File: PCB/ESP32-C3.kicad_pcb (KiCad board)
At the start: 2 copper layers, 28.4 x 27.8 mm, 45 parts, among them J1 HCZZ0039-3, J2 DPS_PPS_Right_Angle, SW2 TS4535TP 250gf 009, U1 USB-C-16P-SMD, U2 BQ24072RGT, U3 ESP32-C3, Y1 40MHz_S3240000151040

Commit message: Neuste Version
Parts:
- added D1: XL-1615RGBC-RF, LEDSMD:LED_0606_1432, F.Cu at (145.6, 80.9)
- added R14: 100_0402, Resistor_SMD:R_0402_1005Metric, F.Cu at (145.5, 79.2)
- added R19: 100_0402, Resistor_SMD:R_0402_1005Metric, F.Cu at (147.5, 80.8)
- added R21: 100_0402, Resistor_SMD:R_0402_1005Metric, F.Cu at (145.8, 82.6)
- moved SW2 1.49 mm to (152.5, 72.4), turned to 0 degrees
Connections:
- U3 pad 18: unconnected-(U3-VDD_SPI-Pad18) -> Rot
- U3 pad 23: unconnected-(U3-SPID-Pad23) -> Blau
- U3 pad 24: unconnected-(U3-SPIQ-Pad24) -> Grün
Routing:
- net Grün: track 0.00 -> 23.2 mm, vias 0 -> 2
- net Blau: track 0.00 -> 17.4 mm, vias 0 -> 2
- net Rot: track 0.00 -> 11.2 mm, vias 0 -> 2
- net EXTI: track 28.6 -> 23.7 mm
- net NCHG: track 37.9 -> 41.3 mm
- net Net-(D1-BK): track 0.00 -> 1.25 mm
- net Net-(D1-GK): track 0.00 -> 1.24 mm
- net Net-(D1-RK): track 0.00 -> 1.20 mm
- net MCU_SCL: track 31.2 -> 31.8 mm
- net NPGOOD: track 29.6 -> 30.1 mm
- net GND: track 41.9 -> 41.8 mm, vias 31 -> 28
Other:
- board text added: "+"
- board text added: "-"
- board text added: "A.S. W-Charger 05.2024"
- board text added: "Button"
- board text added: "Cha."
- board text added: "Charging"
- board text added: "GND SCL SDA"
- board text added: "In."
- board text added: "Input"
- board text added: "TEMP"
- board text added: "|"

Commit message: Update
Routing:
- net GND: vias 28 -> 41

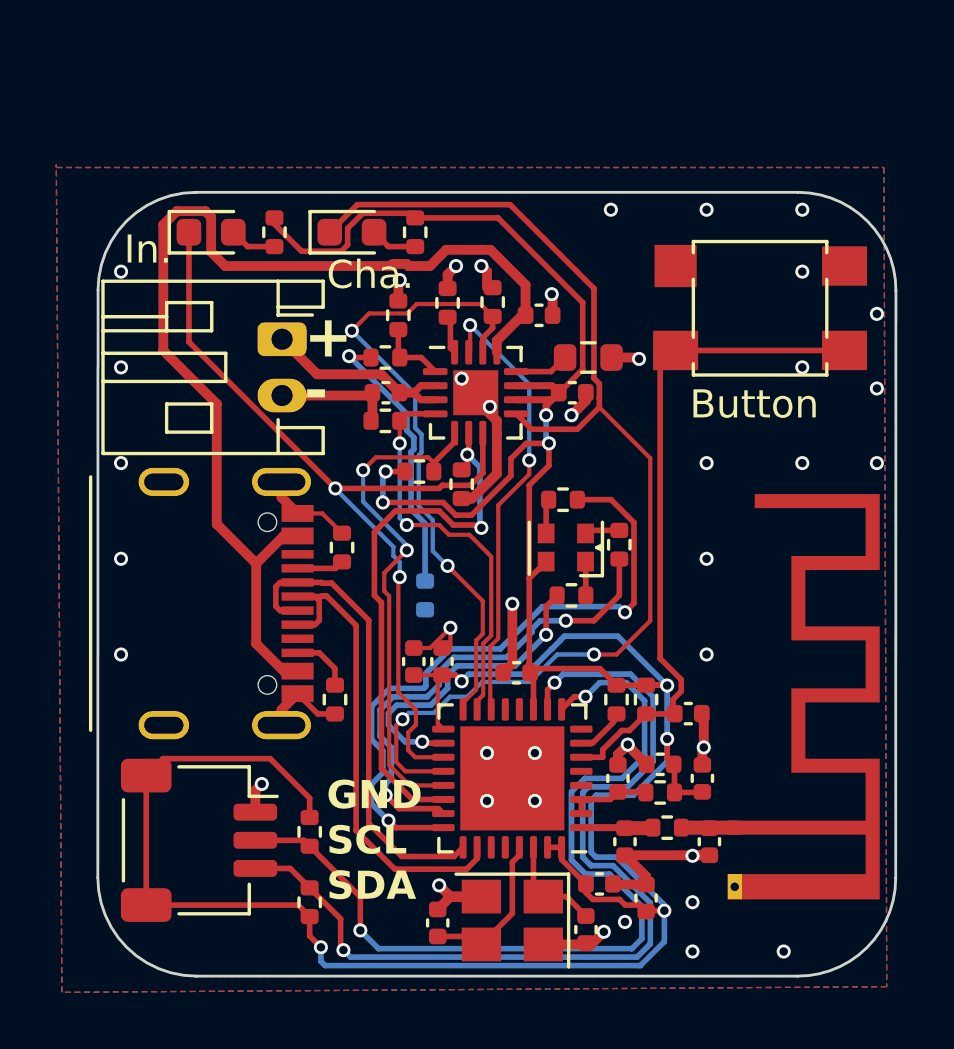
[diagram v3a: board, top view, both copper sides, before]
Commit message: Boot Button hinzugefügt
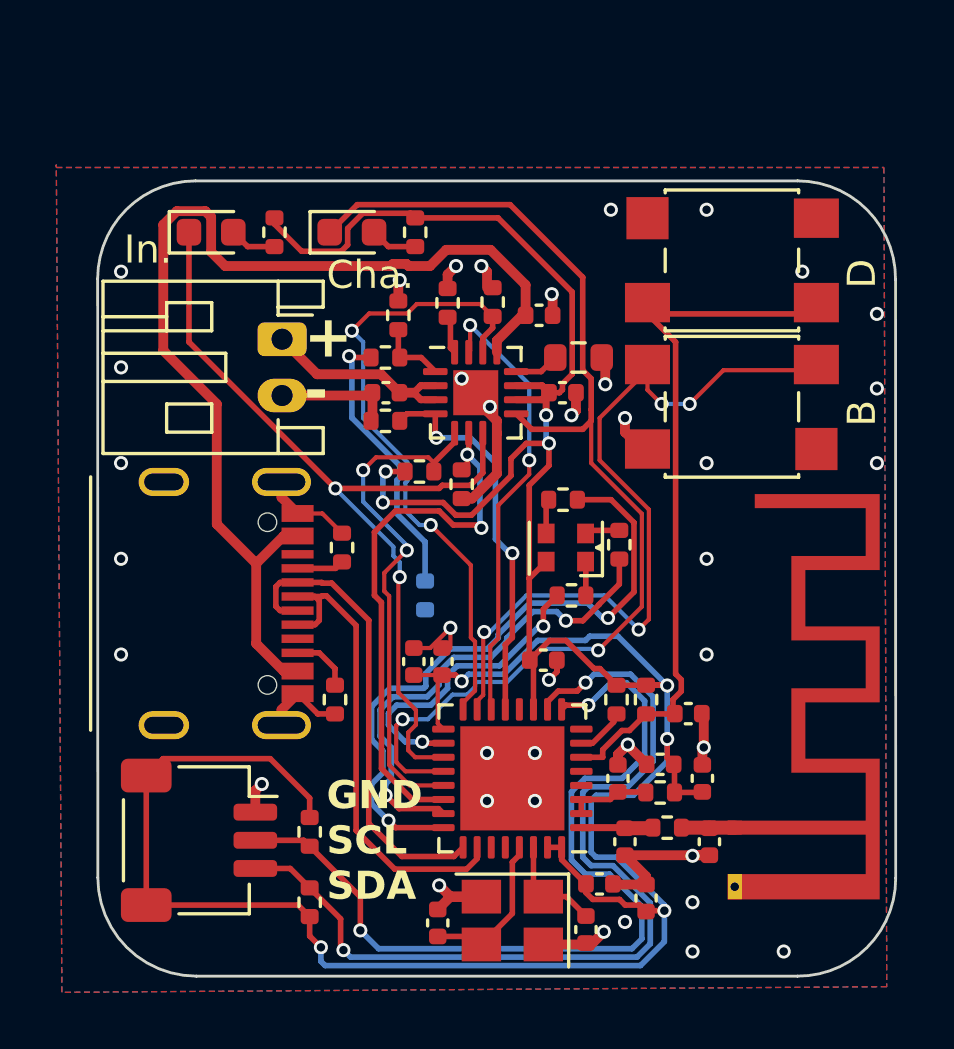
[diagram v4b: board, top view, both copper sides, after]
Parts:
- added SW1: TS-1187A-B-A-B, switch:SW_SPST_TL3305B, F.Cu at (151.5, 70.7)
- D4: value 0603_GREEN -> 0603_WHITE
- R18: value 8k2_0402 -> 5k1_0402
- SW2: value TS4535TP 250gf 009 -> TS-1187A-B-A-B
- moved SW2 3.64 mm to (151.5, 75.9), turned to 180 degrees
- moved C5 1.05 mm to (144.8, 84.9), turned to 180 degrees
- moved C20 0.35 mm to (145.5, 75.4)
- moved R15 0.35 mm to (146.1, 74.2)
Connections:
- SW2 pad 2: EXTI -> Net-(U3-GPIO9)
- U3 pad 13: unconnected-(U3-MTDO-Pad13) -> NCE
- U3 pad 15: NCE -> Net-(U3-GPIO9)
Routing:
- net Net-(U3-GPIO9): track 0.00 -> 27.6 mm, vias 0 -> 4
- net EXTI: track 23.7 -> 25.0 mm
- net NCHG: track 40.8 -> 40.1 mm
- net GND: vias 41 -> 39
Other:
- board size 28.4 x 27.8 mm -> 28.3 x 28.2 mm
- board text added: "B"
- board text added: "D"
- board text removed: "Button"

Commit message: Wichtige Änderungen für die Fertigung
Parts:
- removed R12: 1k_0402, Resistor_SMD:R_0402_1005Metric
- removed R13: 3k_0402_ntc, Resistor_SMD:R_0402_1005Metric
- R11: value 549k_1_0402 -> 10k_0402
- moved R11 1.23 mm to (139.2, 73.8), turned to 180 degrees
- moved SW1 0.10 mm to (151.5, 70.6)
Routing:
- net Net-(R12-Pad2): track 9.99 -> 0.00 mm, vias 1 -> 0
- net TMR: track 22.7 -> 30.7 mm
- net NPGOOD: track 30.1 -> 31.1 mm
- net Net-(U2-TS): track 2.48 -> 1.60 mm
- net EXTI: track 25.0 -> 25.7 mm
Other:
- board size 28.3 x 28.2 mm -> 28.3 x 28.3 mm

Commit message: Kleine Verbesserungen
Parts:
- moved D5 1.85 mm to (139.8, 69.7)
- moved D4 1.81 mm to (134.8, 69.7)
- moved R10 1.66 mm to (136.9, 69.7)
- moved R9 1.65 mm to (141.9, 69.7)
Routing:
- net NPGOOD: track 31.1 -> 32.6 mm
- net NCHG: track 40.1 -> 38.9 mm
- net GND: track 41.9 -> 42.8 mm, vias 39 -> 46
- net +3.3V: track 114.1 -> 113.3 mm
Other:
- board size 28.3 x 28.3 mm -> 28.3 x 28.5 mm
- board text added: "A.S. V1 W-Charger 06.2024"
- board text added: "Char."
- board text added: "Pow."
- board text added: "Power"
- board text removed: "A.S. W-Charger 05.2024"
- board text removed: "Cha."
- board text removed: "In."
- board text removed: "Input"
- board text removed: "TEMP"
- board text removed: "|"

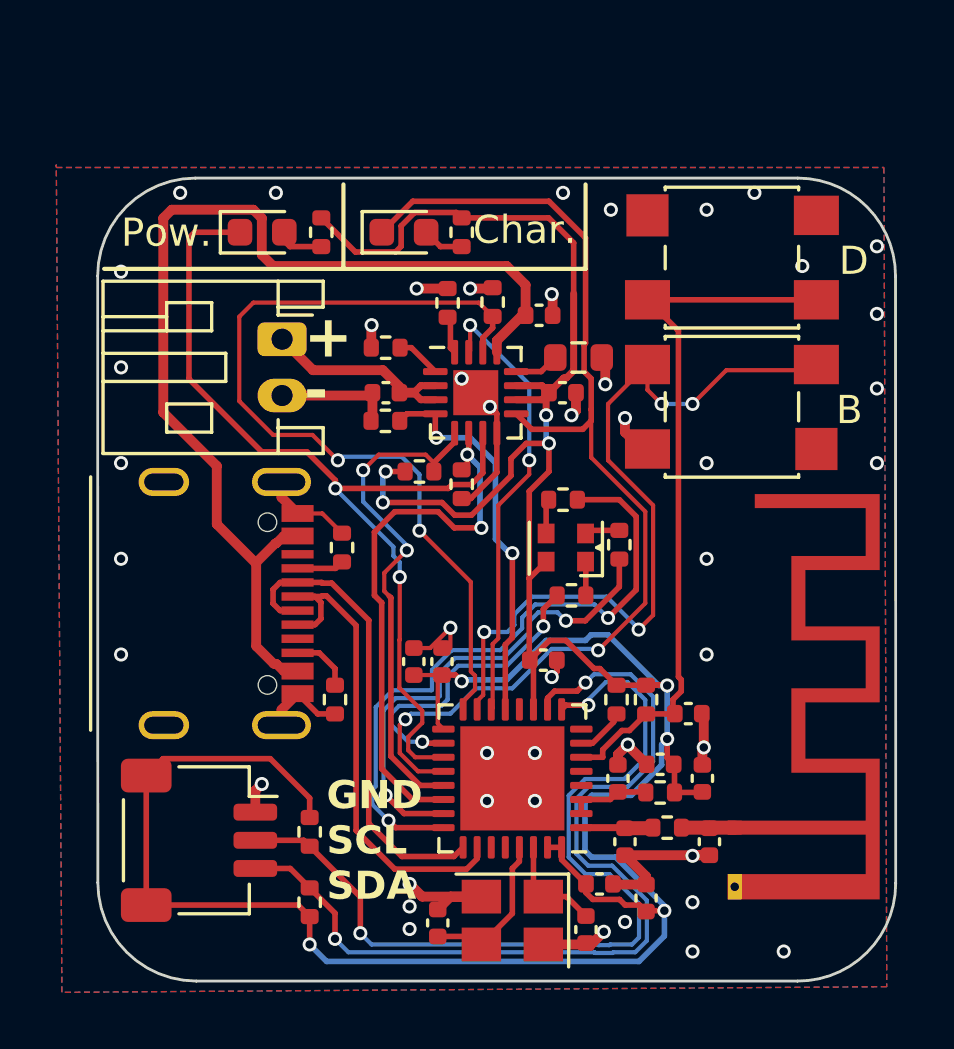
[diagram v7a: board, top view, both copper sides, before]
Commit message: Neuer Charger IC und ein LDO
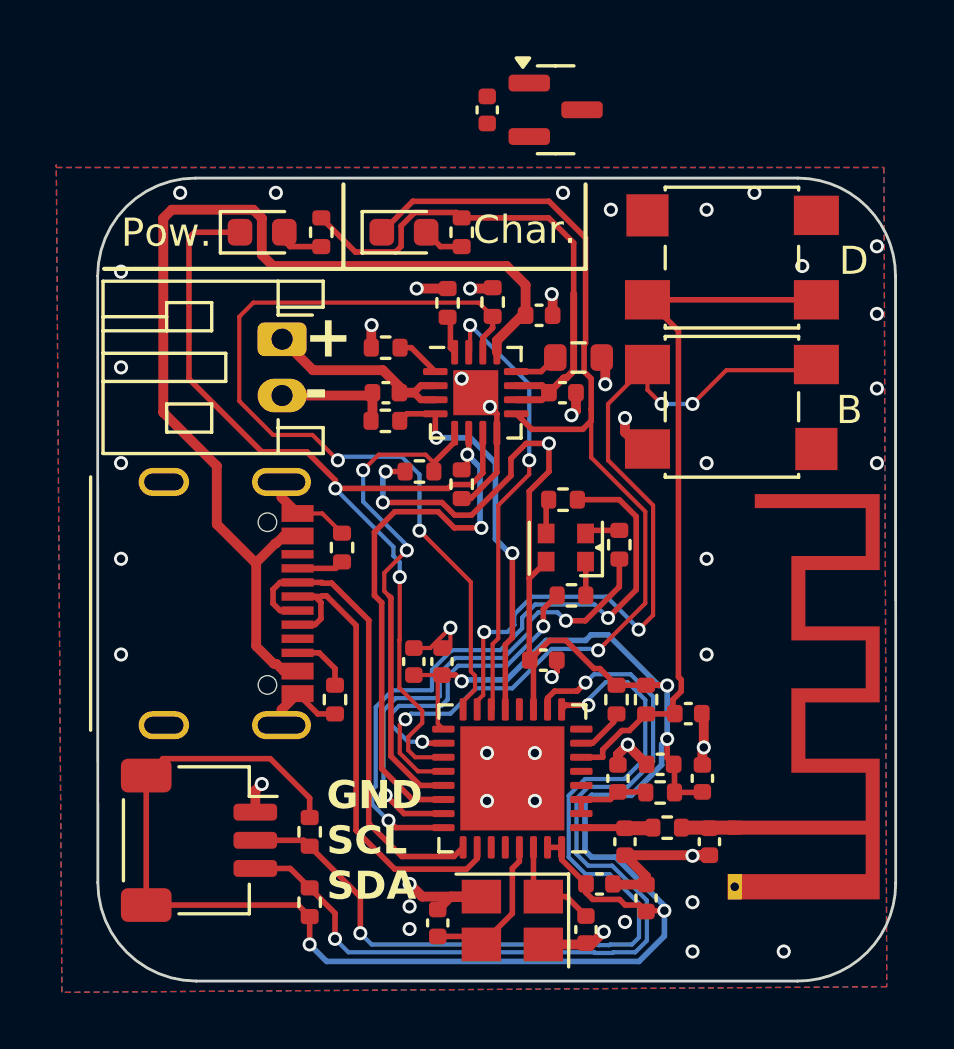
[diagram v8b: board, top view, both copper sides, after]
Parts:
- added C9: 1u_0402_X5R_25V, Capacitor_SMD:C_0402_1005Metric, F.Cu at (142.8, 65.4)
- added U4: DS8242-33SS3, Package_TO_SOT_SMD:SOT-23, F.Cu at (145.2, 65.3)
- U2: value BQ24072RGT -> BQ24073RGTR
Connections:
- C20 pad 1: +3.3V -> Net-(U4-Vin)
- U2 pad 10: +3.3V -> Net-(U4-Vin)
- U2 pad 11: +3.3V -> Net-(U4-Vin)
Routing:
- net +3.3V: track 113.3 -> 111.4 mm, vias 9 -> 8
